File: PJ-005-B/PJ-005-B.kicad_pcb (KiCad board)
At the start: 2 copper layers, 48 x 76 mm, 196 parts, among them IC1 2EDN8534FXTMA1, J1 2 Pin JST XH, J3 Pin Header 4 Pin, J4 3 Pin JST XH, J5 Pin Header 3 Pin, J6 Conn_01x02_Pin, J7 Pin Header 4 Pin, J8 Pin Header 2 Pin, J9 Conn_01x02_Pin, Q1 SIR622DP-T1-RE3, Q2 SIR622DP-T1-RE3, U1 MIC29302WU-TR, U10 AD8608ARUZ-REEL, U11 AD8608ARUZ-REEL, U12 MCP6S91-E/MS, U13 MAX485CSA+T, U2 MIC29302WU-TR, U3 MIC29302WU-TR, U4 LM337IMP/NOPB, U5 REF2033AIDDCR, U6 MIC5365-2.5YC5-TR, U7 MD0105K6-G, U8 B65821C1008T1, U9 TLV365QDBVRQ1

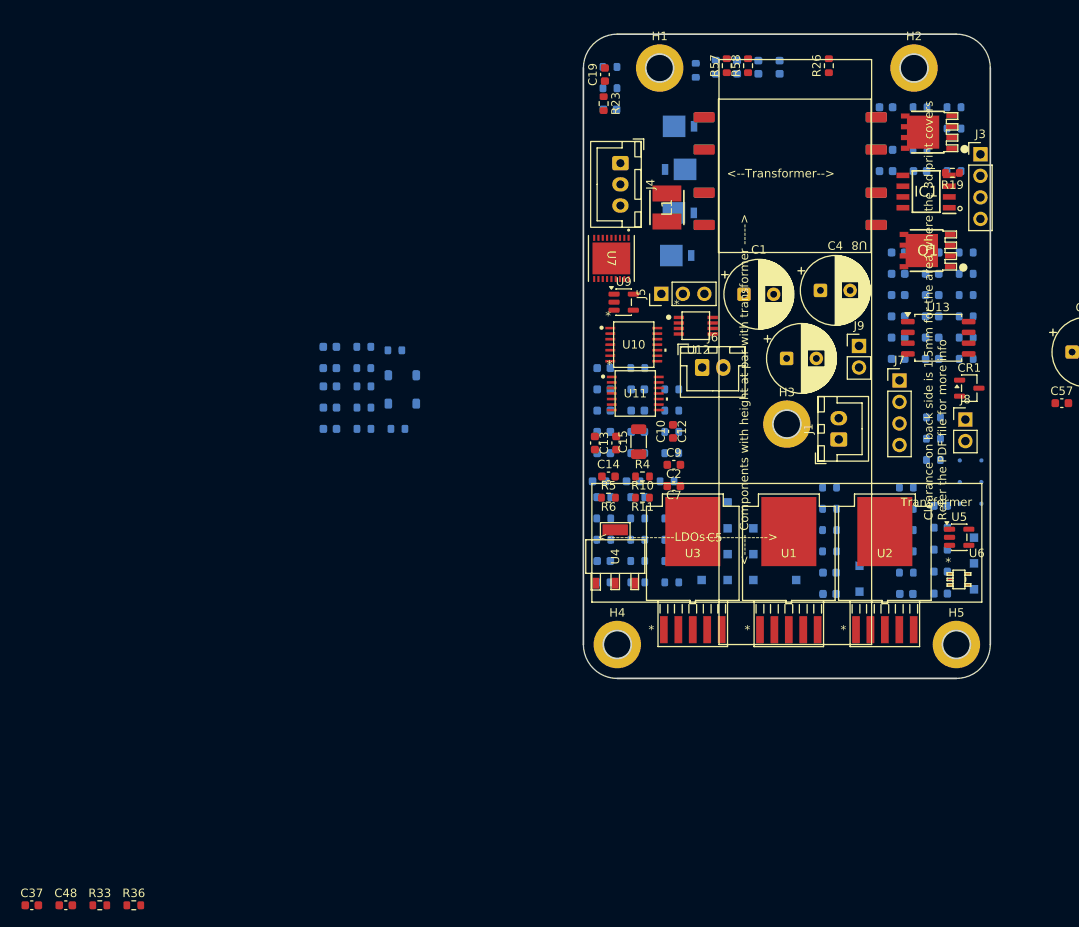
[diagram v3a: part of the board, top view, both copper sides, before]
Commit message: -- Reference Voltage IC removed -- Receiver includes only transmit receive switch and charge amp -- Changes in snubber values -- Changes in pull-up and pull-down resistors
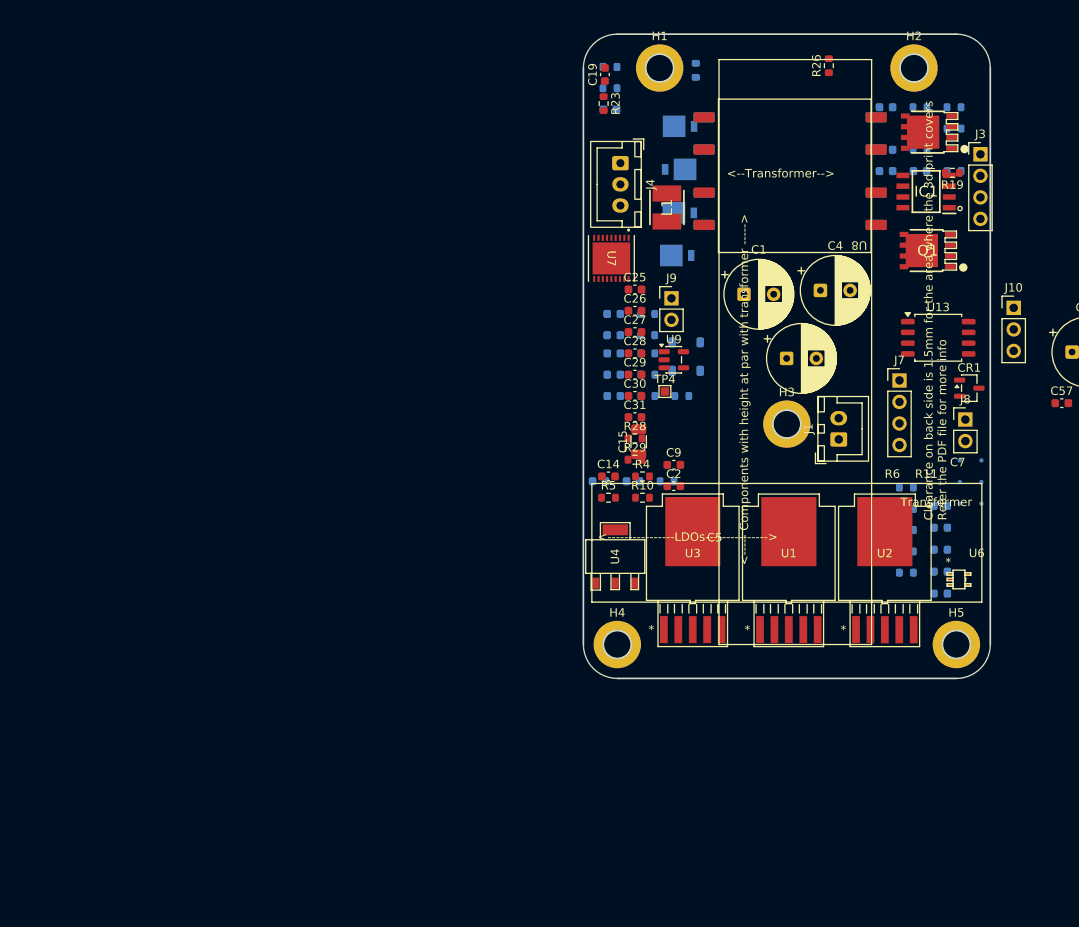
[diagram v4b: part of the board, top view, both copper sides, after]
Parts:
- removed C10, C34, C50, C56: 2.2uF,25V, XaltenFootprints:C0603
- removed C12, C36, C39, C43, C51: 100nF,25V, XaltenFootprints:C0603
- removed C13, C33, C37, C38, C42, C52: 100pF,25V, XaltenFootprints:C0603
- removed C32, C40, C45, C53: 2pF,25V, XaltenFootprints:C0603
- removed C35: 121pF,25V, XaltenFootprints:C0603
- removed C41: 715pF,25V, XaltenFootprints:C0603
- removed C44: 1.21nF,25V, XaltenFootprints:C0603
- removed C46: 1nF,25V, XaltenFootprints:C0603
- removed C47: 3.16nF,25V, XaltenFootprints:C0603
- removed C48: 2.26nF,25V, XaltenFootprints:C0603
- removed C49: 1uF,16V, XaltenFootprints:C0603
- removed J5: Pin Header 3 Pin, Connector_PinHeader_2.54mm:PinHeader_1x03_P2.54mm_Vertical
- removed J6: Conn_01x02_Pin, Connector_JST:JST_XH_B2B-XH-A_1x02_P2.50mm_Vertical
- removed R14, R30, R35, R37, R38, R42, R43, R44, R47, R50, R51, R52, R55, R56, R60, R61: 0R, XaltenFootprints:R0603
- removed R31, R36, R45, R48, R62, R63: 1K,1%, XaltenFootprints:R0603
- removed R32: 3K3,1%, XaltenFootprints:R0603
- removed R33: 8K06,0.1%, XaltenFootprints:R0603
- removed R34: 11K5,1%, XaltenFootprints:R0603
- removed R39: 3K16,0.1%, XaltenFootprints:R0603
- removed R40: 10K,1%, XaltenFootprints:R0603
- removed R41: 4K99,0.1%, XaltenFootprints:R0603
- removed R46: 2K26,0.1%, XaltenFootprints:R0603
- removed R49, R53, R54: 2K67,0.1%, XaltenFootprints:R0603
- removed R57, R58: 10R,1%, XaltenFootprints:R0603
- removed R59: 4K7,1%, XaltenFootprints:R0603
- removed TP1, TP10, TP11, TP12, TP13, TP14, TP15, TP16, TP17, TP18, TP2, TP3, TP5, TP6, TP7, TP8, TP9: TestPoint, TestPoint:TestPoint_Pad_1.0x1.0mm
- removed U10, U11: AD8608ARUZ-REEL, Echosounder Transceiver FP:RU_14_ADI-L
- removed U12: MCP6S91-E/MS, Echosounder Transceiver FP:MSOP8
- removed U5: REF2033AIDDCR, XaltenFootprints:SOT-23-5
- added J10: Conn_01x03_Pin, Connector_PinHeader_2.54mm:PinHeader_1x03_P2.54mm_Vertical, F.Cu at (192.8, 94.3)
- C25, C26, C27, C28, R28, R29, TP4: moved to F.Cu
- C29: value 100nF,25V -> 2.2uF,25V; moved to F.Cu
- C30: value 2.2uF,25V -> 100nF,25V; moved to F.Cu
- C31: value 100nF,25V -> 100pF,25V; moved to F.Cu
- moved D6 33.7 mm to (154.1, 101.7)
- moved D7 33.7 mm to (154.1, 98.4)
- moved R11 33.7 mm to (153.6, 104.7)
- moved C21 33.7 mm to (145.6, 97.5)
- moved C22 33.7 mm to (145.6, 95.0)
- moved C3 33.7 mm to (145.6, 102.2)
- moved C7 33.7 mm to (145.6, 104.7)
- moved C8 33.7 mm to (145.6, 99.7)
- moved R1 33.7 mm to (149.6, 102.2)
- moved R18 33.7 mm to (149.6, 97.5)
- moved R2 33.7 mm to (149.6, 99.7)
- moved R21 33.7 mm to (149.6, 95.0)
- moved R6 33.7 mm to (149.6, 104.7)
- moved TP4 27.1 mm to (151.6, 104.2)
- moved J9 22.8 mm to (152.4, 93.2)
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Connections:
- net /Receiver/Charge Amp + Inverting Amp/CHARGE_AMP_IN renamed Net-(U7-B1)
- C25 pad 1: +3.3V -> +2V5
- C26 pad 2: +3.3V -> +2V5
- C28 pad 2: +3.3V -> +2V5
- C29 pad 1: Net-(C29-Pad1) -> -2V5
- C29 pad 2: Net-(C29-Pad2) -> GND
- C30 pad 1: +3.3V -> GND
- C30 pad 2: GND -> -2V5
- C31 pad 2: +3.3V -> -2V5

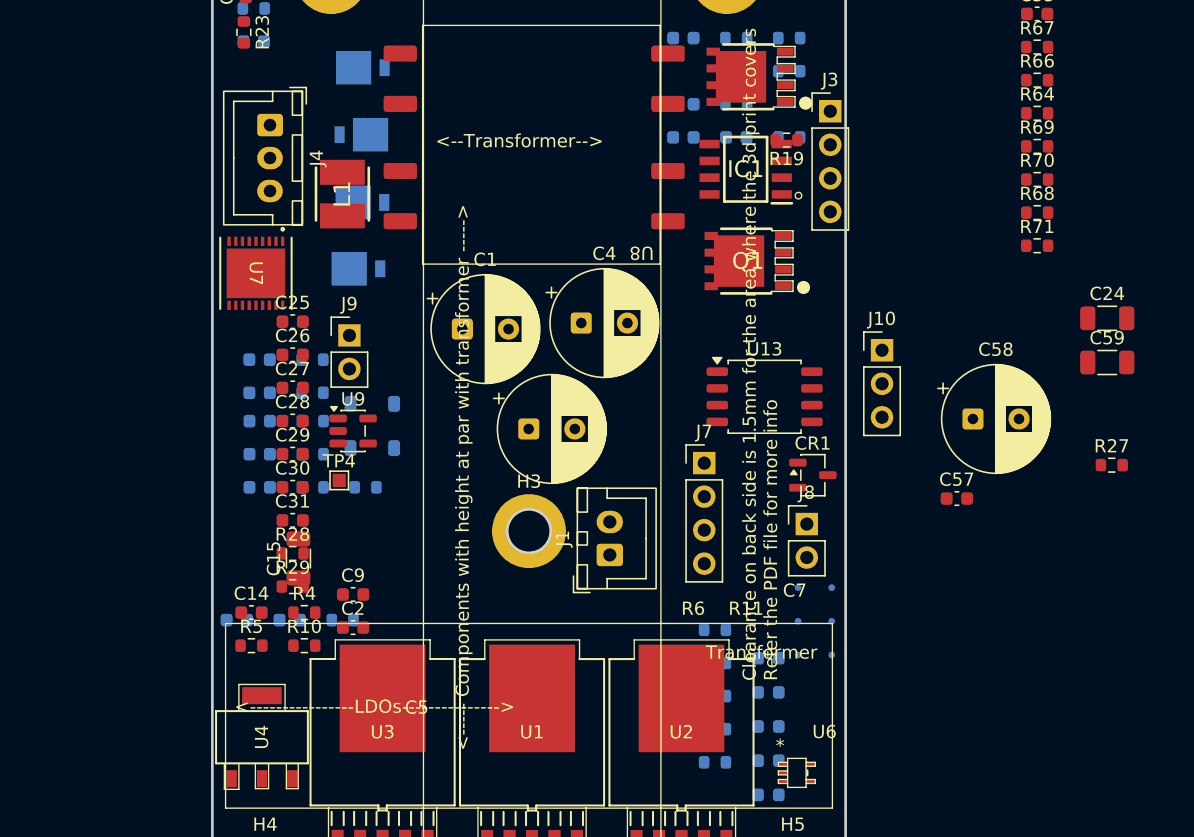
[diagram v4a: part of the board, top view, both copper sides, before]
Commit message: Removed filter, inverting amplifiers, buffer and PGA
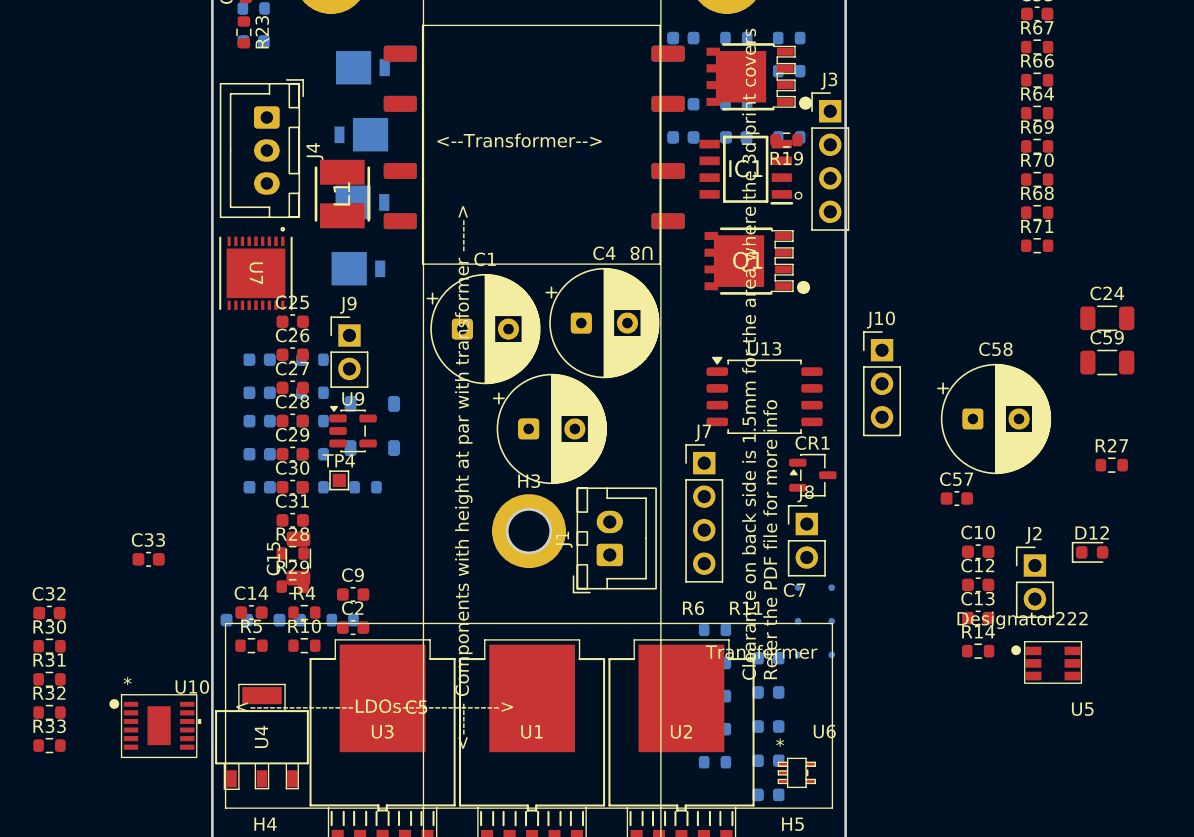
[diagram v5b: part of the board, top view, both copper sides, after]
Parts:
- added C10: 2.2uF,25V, XaltenFootprints:C0603, F.Cu at (200.0, 109.6)
- added C12: 2.2uF,25V, XaltenFootprints:C0603, F.Cu at (200.0, 112.1)
- added C13: 1uF,25V, XaltenFootprints:C0603, F.Cu at (200.0, 114.6)
- added C32: 10uF,25V, XaltenFootprints:C0603, F.Cu at (129.7, 114.2)
- added C33: 10nF,25V, XaltenFootprints:C0603, F.Cu at (137.2, 110.1)
- added D12: GREEN, LED_SMD:LED_0603_1608Metric, F.Cu at (208.7, 109.6)
- added J2: Pin Header 2 Pin, Connector_PinHeader_2.54mm:PinHeader_1x02_P2.54mm_Vertical, F.Cu at (204.3, 110.6)
- added R14: 3K3,1%, XaltenFootprints:R0603, F.Cu at (200.0, 117.1)
- added R30: 12K7,0.1%, XaltenFootprints:R0603, F.Cu at (129.7, 116.7)
- added R31: 12K1,0.1%, XaltenFootprints:R0603, F.Cu at (129.7, 119.2)
- added R32: 0R, XaltenFootprints:R0603, F.Cu at (129.7, 121.7)
- added R33: 0R, XaltenFootprints:R0603, F.Cu at (129.7, 124.3)
- added U10: LT3015EMSE-TRPBF, Echosounder Transceiver FP:MSOP-12, F.Cu at (138.0, 122.8)
- added U5: LM2776DBVR, Echosounder Transceiver FP:SOT23-6, F.Cu at (205.7, 118.0)
- R1: value 390R,1% -> 430R,1%
- R2: value 100R,1% -> 140R,1%
- R8: value 4K7,1% -> 3K3,1%
- moved J4 0.62 mm to (146.1, 76.7)
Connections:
- C11 pad 1: +5V -> +5VA
- C7 pad 1: +6V -> +5VA
- R1 pad 1: +6V -> +5VA
- R8 pad 1: +6V -> +5VA
- U1 pad 4: +6V -> +5VA
- U6 pad 1: +5V -> +5VA
- U6 pad 3: +5V -> +5VA
